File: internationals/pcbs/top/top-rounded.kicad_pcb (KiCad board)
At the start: 2 copper layers, 170 x 147 mm, 86 parts, among them J1 Header-01x08, J10 JST-XH-S4B, J11 JST-XH-B6B, J12 5V-JST-XH-B2B, J13 Header-01x03, J2 5V-JST-XH-B2B, J3 Debug-JST-XH-B3B, J4 5V-JST-XH-B2B, J5 5V-JST-XH-B2B, J6 IMU-UART-JST-XH-B2B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

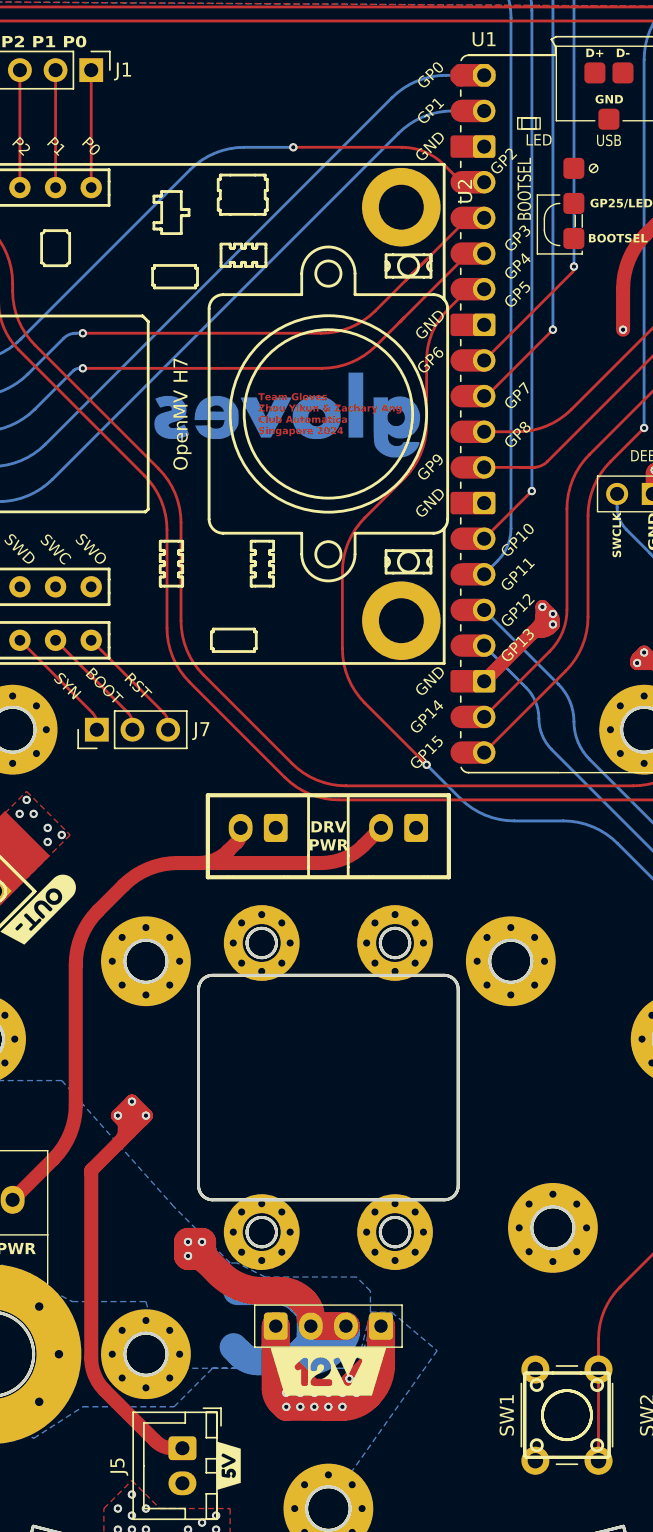
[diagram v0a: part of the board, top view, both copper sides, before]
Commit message: pcbs: feat: add OSHW and Rust Ferris logos
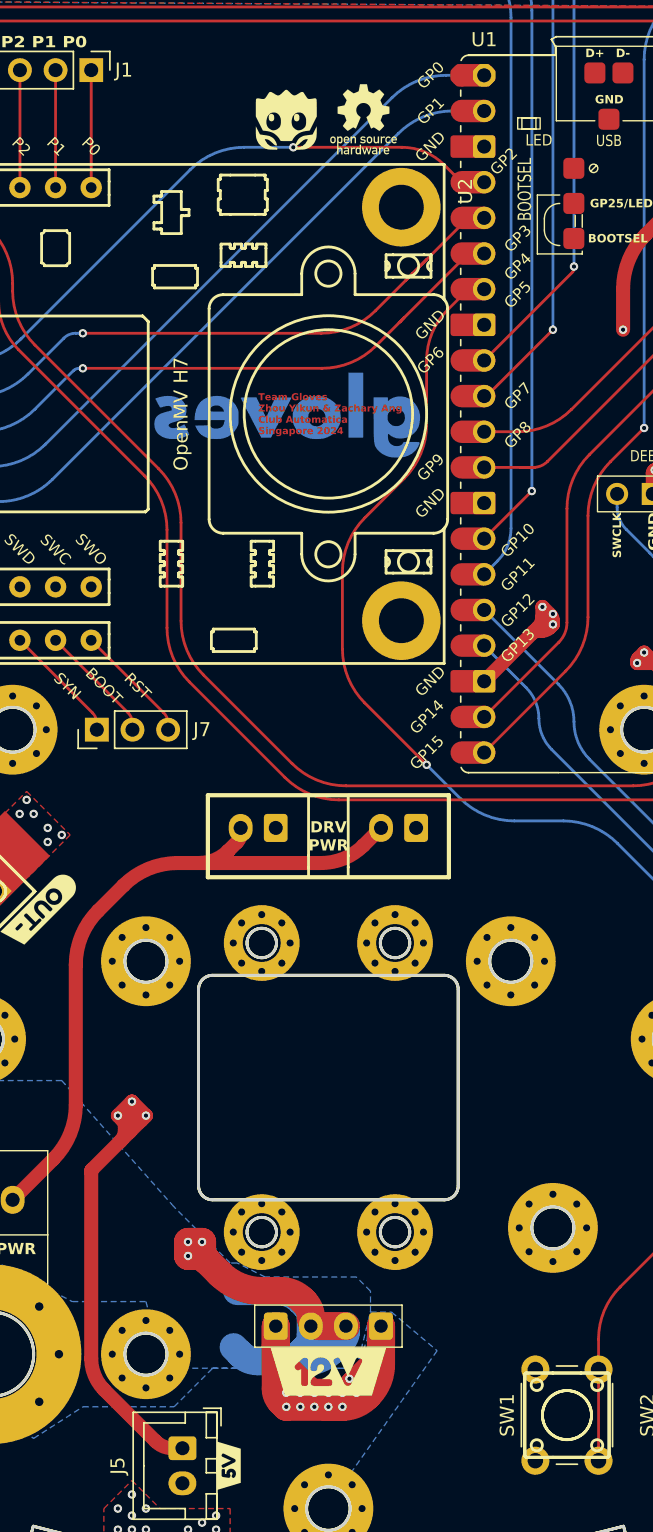
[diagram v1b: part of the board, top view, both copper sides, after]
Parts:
- added G***: LOGO, LOGO, F.Cu at (97.0, 79.0)
- added G***: LOGO, LOGO, F.Cu at (102.5, 79.0)
